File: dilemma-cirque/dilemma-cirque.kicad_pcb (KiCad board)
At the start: 2 copper layers, 37 x 45.1 mm, 9 parts, among them J1 CirqueDB

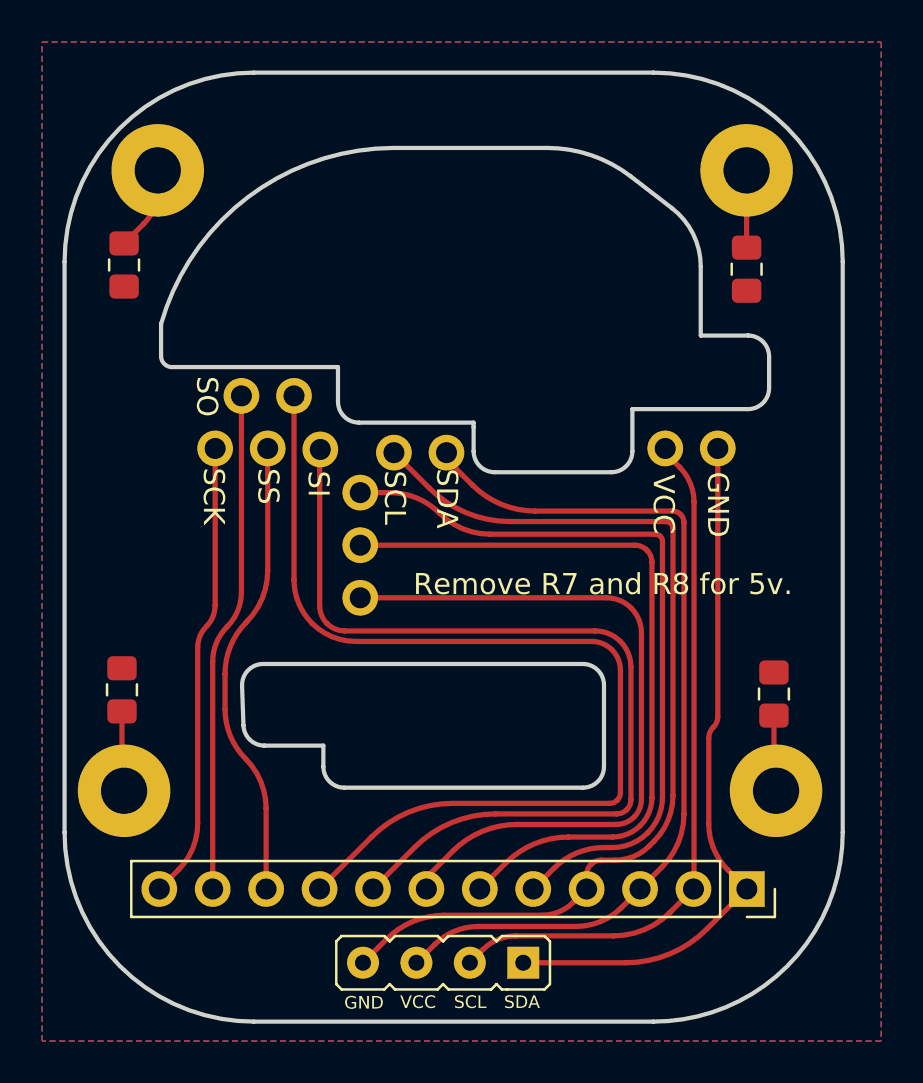
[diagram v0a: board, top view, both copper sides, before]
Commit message: clean up footprints
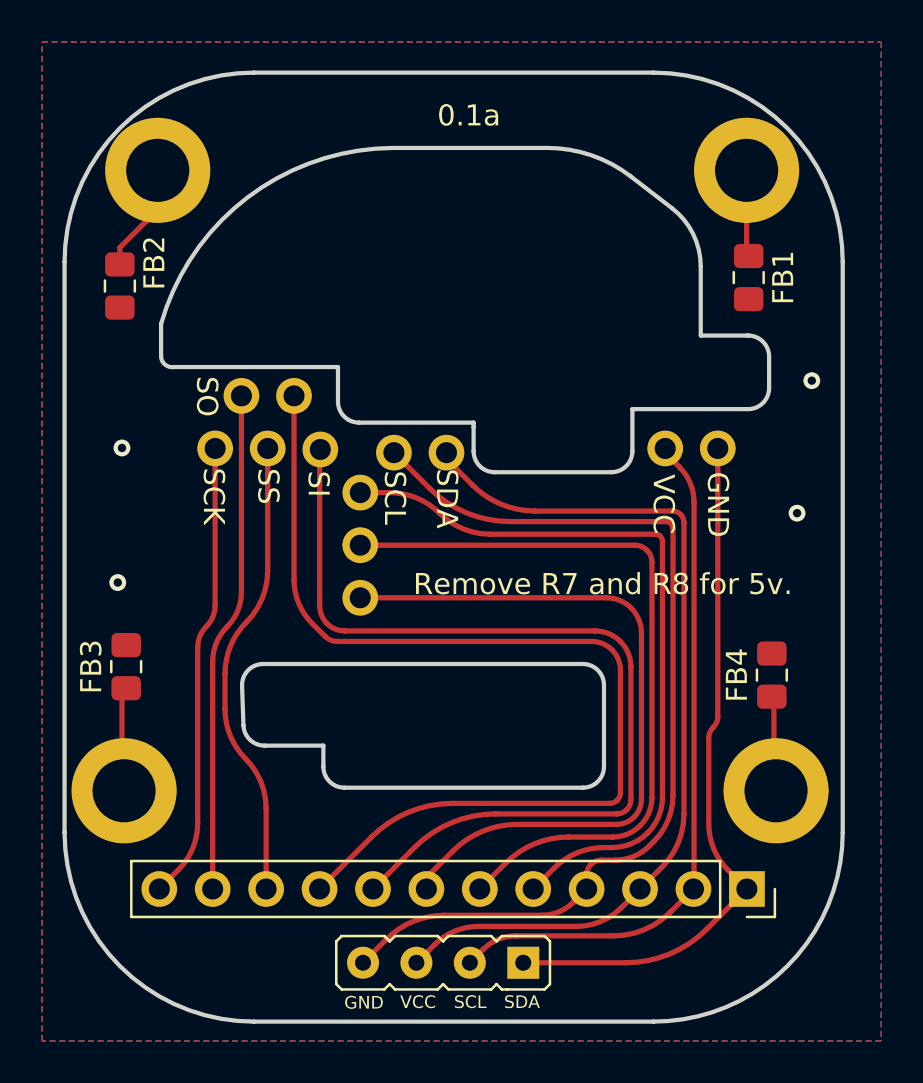
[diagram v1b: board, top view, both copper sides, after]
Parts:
- FB1, FB2, FB3, FB4: footprint BK-CirqueDB:L_0805_2012Metric_Pad1.15x1.40mm_HandSolder -> Inductor_SMD:L_0805_2012Metric_Pad1.15x1.40mm_HandSolder
- H1, H2, H3, H4: footprint BK-CirqueDB:MountingHole_2.2mm_M2_Pad -> footprints:MountingHole_3mm_Pad_thin
- moved FB3 1.12 mm to (130.5, 97.2)
- moved FB2 1.02 mm to (130.2, 79.1)
- moved FB4 0.91 mm to (161.2, 97.6)
- moved FB1 0.41 mm to (160.1, 78.7)
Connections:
- FB1 pad 1: (no net) -> Net-(FB1-Pad1)
- FB2 pad 1: (no net) -> Net-(FB2-Pad1)
- FB3 pad 1: (no net) -> Net-(FB3-Pad1)
- FB4 pad 1: (no net) -> Net-(FB4-Pad1)
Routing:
- net Net-(FB3-Pad1): track 3.81 -> 4.99 mm
- net Net-(FB2-Pad1): track 4.03 -> 5.12 mm
- net Net-(FB4-Pad1): track 3.61 -> 4.55 mm
- net GND: vias 0 -> 4
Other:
- board text added: "0.1a"
